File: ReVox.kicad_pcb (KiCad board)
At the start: 2 copper layers, 60.8 x 86.2 mm, 45 parts, among them CN1 EXPANSION_PORT, CN2 AUDIO_OUT, CN3 AUDIO_OUT, CN4 CN_RAW_DAC, U1 GAL20V8, U2 74LS273, U3 LM386

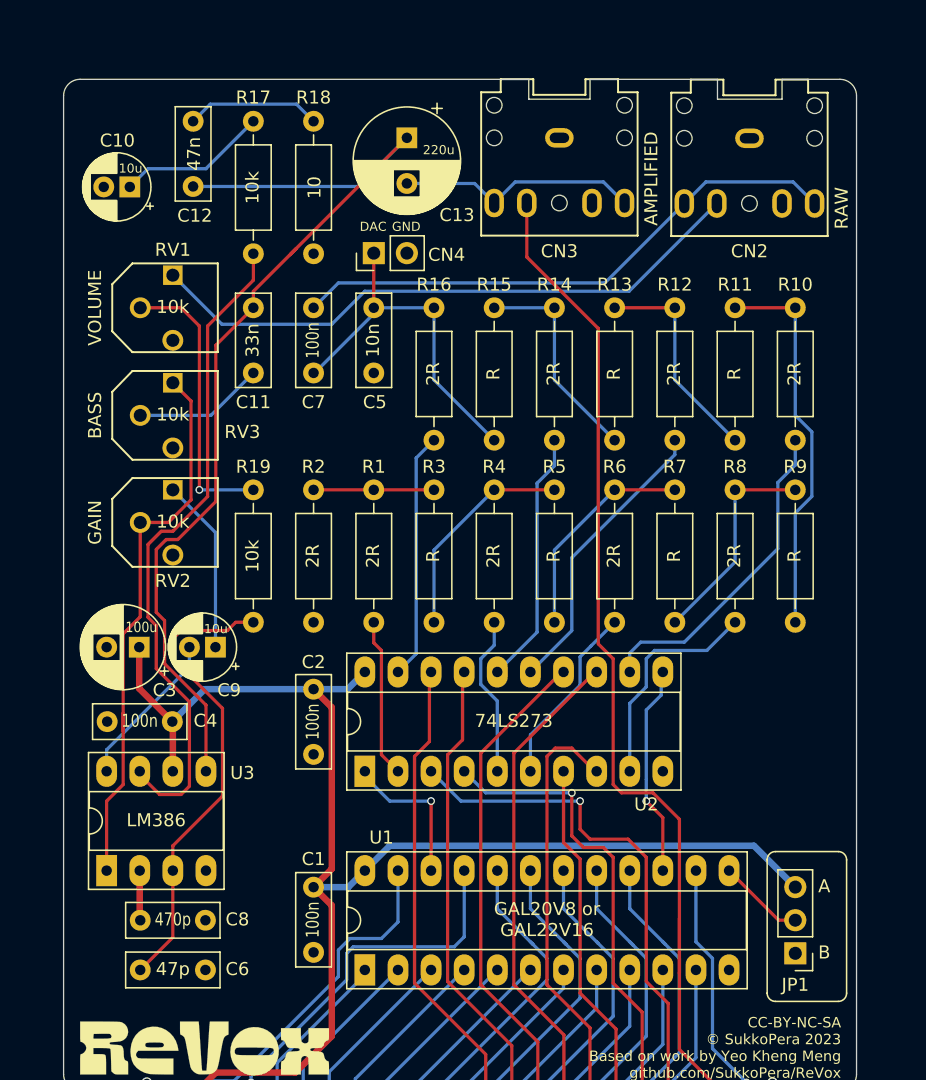
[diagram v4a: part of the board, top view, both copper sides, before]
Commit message: Simpler amplifier circuit
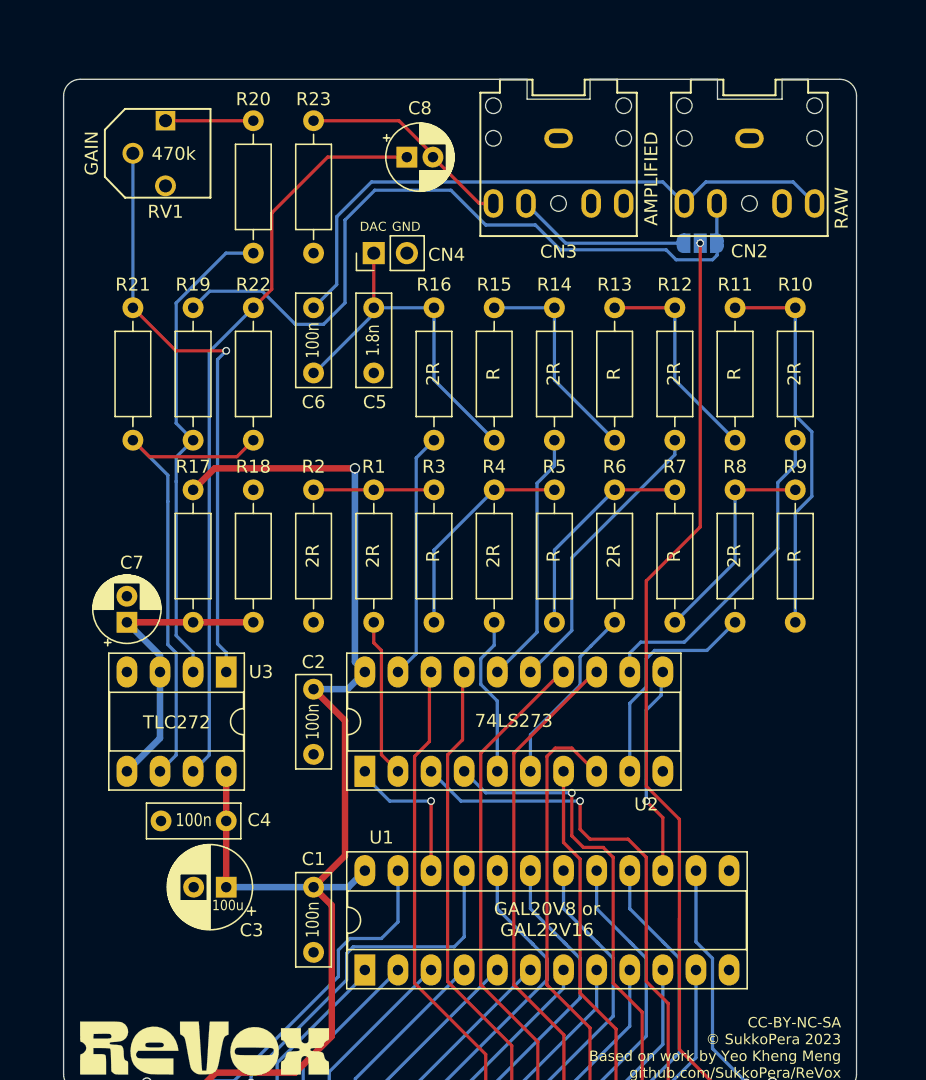
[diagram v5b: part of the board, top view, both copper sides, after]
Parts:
- removed C10, C9: 10u, Capacitor_THT:CP_Radial_D5.0mm_P2.00mm
- removed C11: 33n, Capacitor_THT:C_Disc_D7.0mm_W2.5mm_P5.00mm
- removed C12: 47n, Capacitor_THT:C_Disc_D7.0mm_W2.5mm_P5.00mm
- removed C13: 220u, Capacitor_THT:CP_Radial_D8.0mm_P3.50mm
- removed the C6 at (132.7, 130.2)
- removed the RV1 at (128.9, 79.4)
- removed RV3: 10k, ReVox:Pot_Bourns_3306P
- added C7: 10u, Capacitor_THT:CP_Radial_D5.0mm_P2.00mm, F.Cu at (126.7, 103.5)
- added R20: 100k, Resistor_THT:R_Axial_DIN0207_L6.3mm_D2.5mm_P10.16mm_Horizontal, F.Cu at (136.4, 65.0)
- added R21: 11k, Resistor_THT:R_Axial_DIN0207_L6.3mm_D2.5mm_P10.16mm_Horizontal, F.Cu at (127.1, 79.4)
- added R22: 11k, Resistor_THT:R_Axial_DIN0207_L6.3mm_D2.5mm_P10.16mm_Horizontal, F.Cu at (136.4, 79.4)
- added R23: 11k, Resistor_THT:R_Axial_DIN0207_L6.3mm_D2.5mm_P10.16mm_Horizontal, F.Cu at (141.0, 65.0)
- C5: value 10n -> 1.8n
- C8: value 470p -> 10u; footprint Capacitor_THT:C_Disc_D7.0mm_W2.5mm_P5.00mm -> Capacitor_THT:CP_Radial_D5.0mm_P2.00mm
- JP1: value JMP_ADDRESS -> JMP_AUDIO_SRC; footprint Connector_PinHeader_2.54mm:PinHeader_1x03_P2.54mm_Vertical -> Jumper:SolderJumper-3_P1.3mm_Open_RoundedPad1.0x1.5mm; moved to B.Cu
- R17: value 10k -> 3.3k
- R18: value 10 -> 2.2k
- R19: value 10k -> 100k
- RV1: renamed from RV2; value 10k -> 470k
- U3: value LM386 -> TLC272
- moved C8 60.6 mm to (148.1, 67.8), turned to 0 degrees
- moved JP1 55.0 mm to (170.6, 74.4), turned to 0 degrees
- moved R17 28.7 mm to (131.7, 93.3)
- moved R18 28.7 mm to (136.4, 103.5)
- moved RV1 28.3 mm to (128.4, 67.5)
- moved C3 19.6 mm to (134.3, 123.8)
- moved U3 17.8 mm to (134.3, 107.3), turned to 270 degrees
- moved R19 14.7 mm to (131.7, 89.5)
- moved C4 8.67 mm to (134.3, 118.7)
- moved CN3 0.07 mm to (159.8, 66.4)
- renumbered C7 to C6
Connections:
- net /aa renamed Net-(CN1-PadAA)
- net /aec renamed Net-(CN1-Pad22)
- net /ba renamed Net-(CN1-Pad13)
- net /bb renamed Net-(CN1-PadBB)
- net /c1hi renamed Net-(CN1-Pad6)
- net /c1lo renamed Net-(CN1-PadB)
- net /c2hi renamed Net-(CN1-Pad8)
- net /c2lo renamed Net-(CN1-Pad7)
- net /mux renamed Net-(CN1-Pad12)
- net /phi0 renamed Net-(CN1-PadE)
- net /z renamed Net-(CN1-PadZ)
- net /~cas renamed Net-(CN1-Pad11)
- net /~cs0 renamed Net-(CN1-Pad10)
- net /~cs1 renamed Net-(CN1-Pad9)
- net /~irq renamed Net-(CN1-Pad4)
- net /~ras renamed Net-(CN1-PadD)
- C8 pad 1: GND -> Net-(C8-Pad1)
- C8 pad 2: Net-(C8-Pad2) -> /amplified_audio
- CN3 pad TN: /ext_audio -> Net-(CN3-PadTN)
- JP1 pad 1: GND -> Net-(CN3-PadTN)
- JP1 pad 2: Net-(JP1-Pad2) -> /ext_audio
- JP1 pad 3: +5V -> /amplifier_in
- R17 pad 1: Net-(C10-Pad1) -> +5V
- R17 pad 2: Net-(R17-Pad2) -> VCOM
- R18 pad 1: GND -> VCOM
- R18 pad 2: Net-(C12-Pad2) -> GND
- R19 pad 1: Net-(C6-Pad2) -> Net-(R19-Pad1)
- R19 pad 2: Net-(R19-Pad2) -> /amplifier_in
- U1 pad 13: Net-(JP1-Pad2) -> Net-(U1-Pad13)
- U3 pad 2: Net-(C8-Pad2) -> Net-(R19-Pad1)
- U3 pad 3: Net-(C6-Pad2) -> VCOM
- U3 pad 5: Net-(C11-Pad1) -> VCOM
- U3 pad 6: +5V -> Net-(R21-Pad2)
- U3 pad 7: Net-(R17-Pad2) -> Net-(C8-Pad1)
- U3 pad 8: Net-(C9-Pad2) -> +5V
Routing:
- net Net-(C11-Pad1): track 77.3 -> 0.00 mm
- net Net-(C8-Pad1): track 0.00 -> 56.9 mm
- net Net-(R17-Pad2): track 51.0 -> 0.00 mm
- net Net-(R21-Pad2): track 0.00 -> 37.6 mm
- net Net-(R19-Pad1): track 0.00 -> 37.4 mm
- net Net-(C6-Pad2): track 36.3 -> 0.00 mm
- net VCOM: track 0.00 -> 23.7 mm
- net Net-(R19-Pad2): track 21.8 -> 0.00 mm, vias 1 -> 0
- net Net-(CN3-PadTN): track 0.00 -> 13.6 mm
- net Net-(C9-Pad2): track 12.2 -> 0.00 mm
- net +5V: track 117.9 -> 105.8 mm, vias 0 -> 1
- net Net-(C10-Pad1): track 11.6 -> 0.00 mm
- net Net-(C12-Pad2): track 10.3 -> 0.00 mm
- net Net-(C11-Pad2): track 10.0 -> 0.00 mm
- net /amplifier_in: track 47.1 -> 56.1 mm
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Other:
- outline, holes or cut-outs redrawn
- board text removed: "A"
- board text removed: "B"
- board text removed: "BASS"
- board text removed: "VOLUME"

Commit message: Move some stuff
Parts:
- moved R19 4.62 mm to (127.1, 89.5)
- moved R21 4.62 mm to (131.7, 79.4)
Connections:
- U3 pad 1: Net-(R21-Pad1) -> Net-(C8-Pad1)
- U3 pad 2: Net-(R19-Pad1) -> Net-(R21-Pad2)
- U3 pad 6: Net-(R21-Pad2) -> Net-(R19-Pad1)
- U3 pad 7: Net-(C8-Pad1) -> Net-(R21-Pad1)
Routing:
- net Net-(R21-Pad2): track 37.6 -> 23.4 mm
- net Net-(C8-Pad1): track 56.9 -> 48.3 mm
- net Net-(R19-Pad1): track 37.4 -> 45.5 mm
- net Net-(R21-Pad1): track 45.6 -> 51.9 mm, vias 1 -> 0
- net /amplifier_in: track 56.1 -> 60.7 mm

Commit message: Routing done
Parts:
- R21, R22: value 11k -> 100k
- moved JP1 5.59 mm to (170.6, 68.8)
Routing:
- net /amplified_audio: track 16.5 -> 27.9 mm
- net /amplifier_in: track 60.7 -> 54.4 mm
- net /ext_audio: track 77.9 -> 83.4 mm
- net /analog_audio: track 47.5 -> 44.2 mm
- net +5V: track 105.8 -> 107.6 mm
- net Net-(R21-Pad1): track 51.9 -> 50.9 mm
- net Net-(CN3-PadTN): track 13.6 -> 13.1 mm

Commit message: Final touches
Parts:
- CN2: value AUDIO_OUT -> RAW_OUT
- CN3: value AUDIO_OUT -> AMP_OUT
- R23: value 11k -> 10k
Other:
- board text added: "AMP"
